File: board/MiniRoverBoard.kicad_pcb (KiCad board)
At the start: 2 copper layers, 49 parts, among them J1 DEBUG, Q1 NMOS, Q2 BSS138, U2 OKI, U3 Opamp_Dual, U4 LT1910, U7 ESP32-S2-DEVKITM-1U, U8 Opamp_Dual

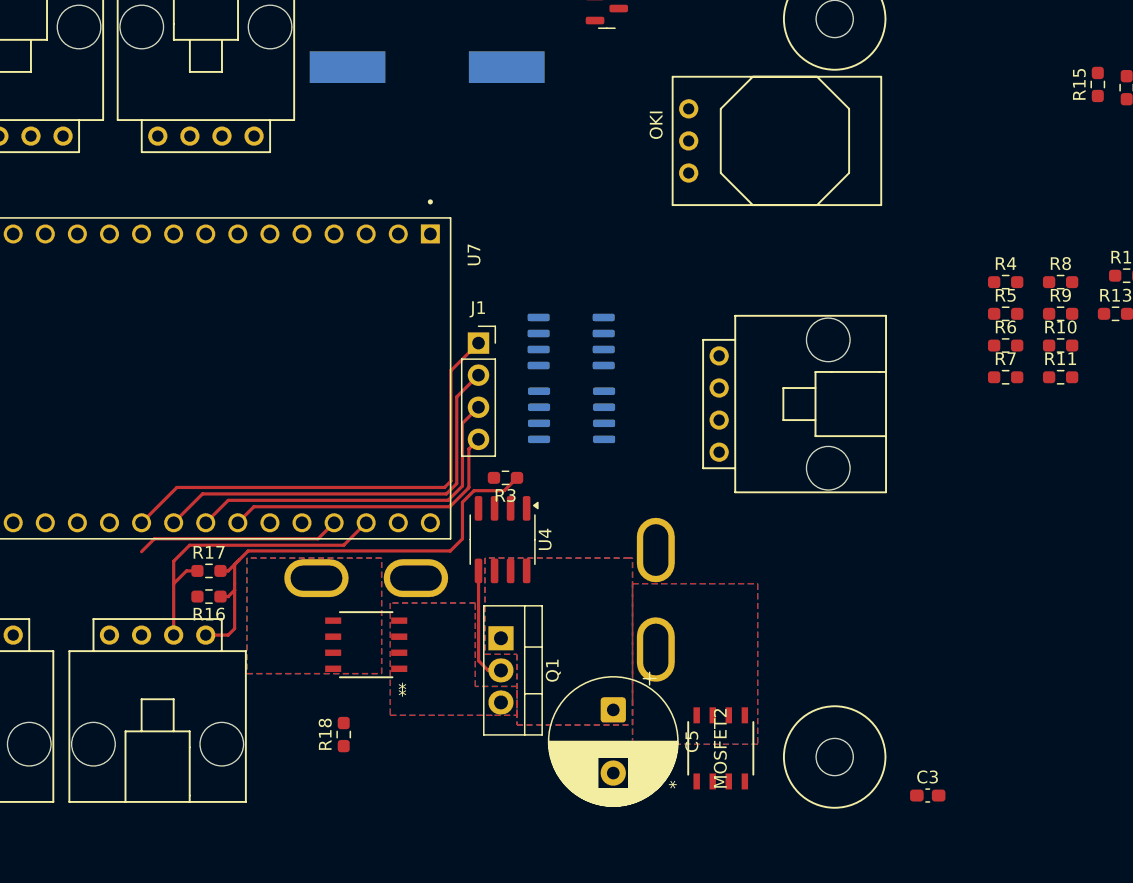
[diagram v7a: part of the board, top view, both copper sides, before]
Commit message: Add power planes
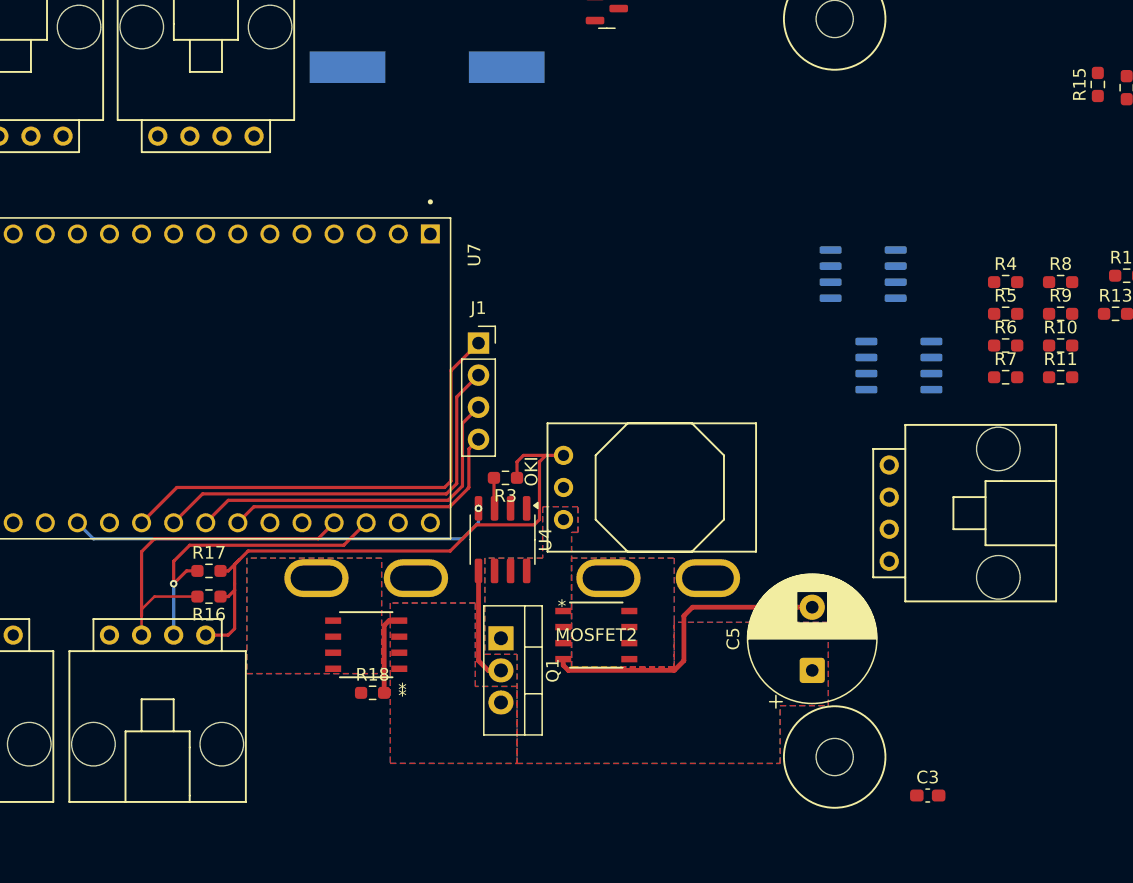
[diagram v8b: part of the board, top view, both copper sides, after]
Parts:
- moved U2 29.2 mm to (122.3, 78.5)
- moved U3 26.0 mm to (148.8, 66.3)
- moved U8 25.6 mm to (146.0, 59.1)
- moved C5 16.1 mm to (142.0, 90.4), turned to 90 degrees
- moved Conn4 16.0 mm to (148.1, 74.2)
- moved MOSFET2 13.3 mm to (124.9, 87.6), turned to 0 degrees
- moved Conn2 5.14 mm to (134.0, 83.0), turned to 90 degrees
- moved R18 4.02 mm to (107.2, 92.2), turned to 0 degrees
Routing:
- net ESC_Enable: track 0.00 -> 33.9 mm, vias 0 -> 1
- net Net-(MOSFET2-GATE): track 0.00 -> 24.5 mm
- net SCL: track 16.2 -> 28.1 mm
- net +5V: track 37.7 -> 46.8 mm
- net Net-(MOSFET1-GATE): track 0.00 -> 6.69 mm
- net Net-(U4-FAULT): track 0.00 -> 2.44 mm
- net SDA: vias 0 -> 1
